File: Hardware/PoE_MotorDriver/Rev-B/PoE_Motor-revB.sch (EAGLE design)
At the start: 87 parts, among them IC2 ATMEGA32U4-MU, J6 10103594-0001LF, SW1 SPST_TACT-KMR2, T1 DMG3415U, U2 SPX3819-3.3, U3 LMV358IDGKR, U4 W5500, U8 DRV8871, U9 DRV8871, X2 J1011FHANRUN, X3 DCMOTOR, X4 DCMOTOR, Y4 8MHz

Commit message: HEEP-614 finished rev b motor driver
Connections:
- removed net 10: J4.1, U8.IN1
- removed net 5: J2.1, U8.IN2
- removed net 6: J5.1, U9.IN1
- removed net 9: J3.1, U9.IN2
- net EN1: now also D1.A, J2.1, U8.IN2
- net EN2: now also D2.A, J4.1, U8.IN1
- net EN3: now also D3.A, J3.1, U9.IN2
- net EN4: now also D4.A, J5.1, U9.IN1
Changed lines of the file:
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@@
 </segment>
 </net>
-<net name="5" class="0">
+<net name="EN1" class="0">
 <segment>
 <pinref part="U8" gate="G$1" pin="IN2"/>
-<wire x1="375.92" y1="215.9" x2="353.06" y2="215.9" width="0.1524" layer="91"/>
+<wire x1="375.92" y1="215.9" x2="365.76" y2="215.9" width="0.1524" layer="91"/>
 <pinref part="J2" gate="G$1" pin="1"/>
+<label x="360.68" y="215.9" size="1.778" layer="95"/>
+<pinref part="D1" gate="G$1" pin="A"/>
+<wire x1="365.76" y1="215.9" x2="353.06" y2="215.9" width="0.1524" layer="91"/>
+<junction x="365.76" y="215.9"/>
 </segment>
 </net>
-<net name="10" class="0">
+<net name="EN2" class="0">
 <segment>
 <pinref part="U8" gate="G$1" pin="IN1"/>
-<wire x1="375.92" y1="213.36" x2="353.06" y2="213.36" width="0.1524" layer="91"/>
+<wire x1="375.92" y1="213.36" x2="365.76" y2="213.36" width="0.1524" layer="91"/>
 <label x="360.68" y="213.36" size="1.778" layer="95"/>
 <pinref part="J4" gate="G$1" pin="1"/>
+<pinref part="D2" gate="G$1" pin="A"/>
+<wire x1="365.76" y1="213.36" x2="353.06" y2="213.36" width="0.1524" layer="91"/>
+<junction x="365.76" y="213.36"/>
 </segment>
 </net>
-<net name="9" class="0">
+<net name="EN3" class="0">
 <segment>
 <pinref part="U9" gate="G$1" pin="IN2"/>
-<wire x1="373.38" y1="167.64" x2="347.98" y2="167.64" width="0.1524" layer="91"/>
+<wire x1="373.38" y1="167.64" x2="358.14" y2="167.64" width="0.1524" layer="91"/>
 <label x="360.68" y="167.64" size="1.778" layer="95"/>
 <pinref part="J3" gate="G$1" pin="1"/>
+<pinref part="D3" gate="G$1" pin="A"/>
+<wire x1="358.14" y1="167.64" x2="347.98" y2="167.64" width="0.1524" layer="91"/>
+<junction x="358.14" y="167.64"/>
 </segment>
 </net>
-<net name="6" class="0">
+<net name="EN4" class="0">
 <segment>
 <pinref part="U9" gate="G$1" pin="IN1"/>
-<wire x1="373.38" y1="165.1" x2="347.98" y2="165.1" width="0.1524" layer="91"/>
+<wire x1="373.38" y1="165.1" x2="358.14" y2="165.1" width="0.1524" layer="91"/>
 <label x="360.68" y="165.1" size="1.778" layer="95"/>
 <pinref part="J5" gate="G$1" pin="1"/>
+<pinref part="D4" gate="G$1" pin="A"/>
+<wire x1="358.14" y1="165.1" x2="347.98" y2="165.1" width="0.1524" layer="91"/>
+<junction x="358.14" y="165.1"/>
 </segment>
 </net>

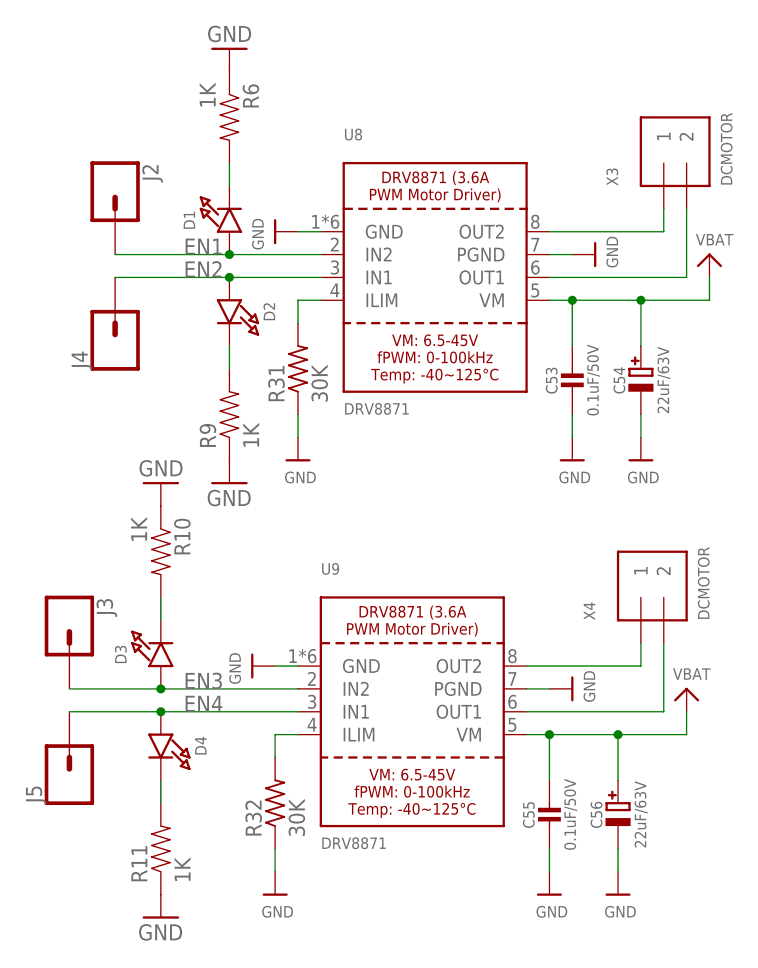
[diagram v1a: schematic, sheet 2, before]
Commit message: HEEP-651 updated capacitor voltage ratings to reflect true minimum requirements
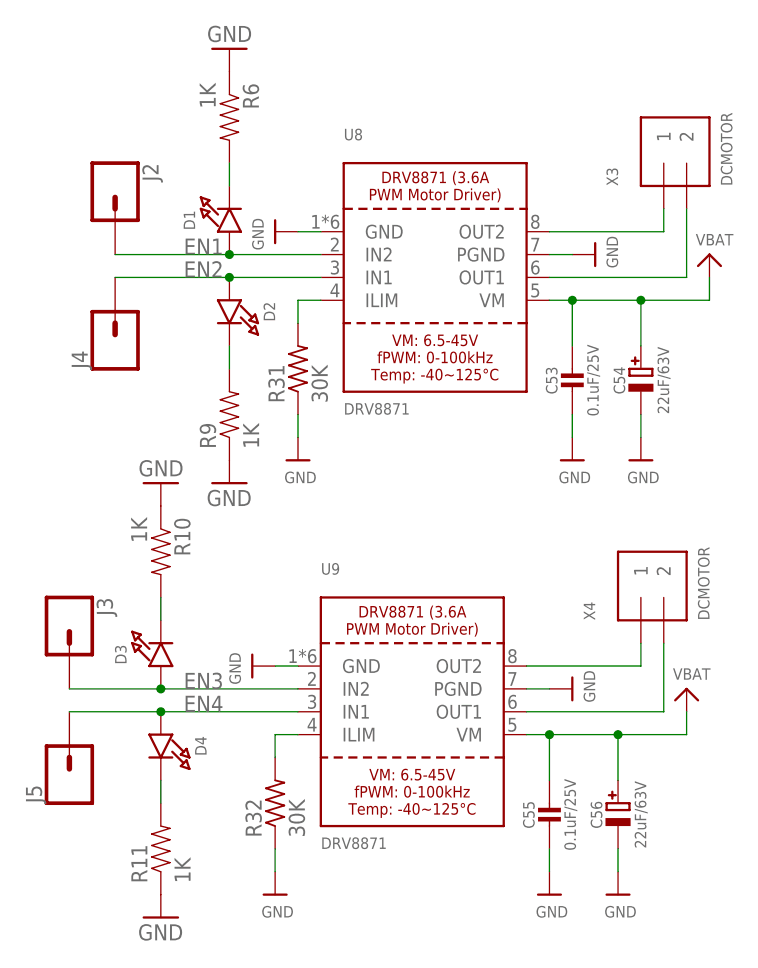
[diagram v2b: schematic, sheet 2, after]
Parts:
- C4: value 10µF 50V -> 10µF 25V
- C53, C55: value 0.1uF/50V -> 0.1uF/25V
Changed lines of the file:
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@@
 <part name="P+2" library="supply1" deviceset="+5V" device=""/>
 <part name="U$19" library="Heep" deviceset="BUCK_CONVERTER" device=""/>
-<part name="C4" library="microbuilder" deviceset="CAP_CERAMIC" device="0603MINI" value="10µF 50V"/>
+<part name="C4" library="microbuilder" deviceset="CAP_CERAMIC" device="0603MINI" value="10µF 25V"/>
 <part name="U$20" library="microbuilder" deviceset="GND" device=""/>
 <part name="U$22" library="microbuilder" deviceset="GND" device=""/>
@@
 <part name="+3V13" library="supply1" deviceset="+3V3" device=""/>
 <part name="U8" library="microbuilder" deviceset="DRV8871" device="" value="DRV8871"/>
-<part name="C53" library="microbuilder" deviceset="CAP_CERAMIC" device="0603_NO" value="0.1uF/50V"/>
+<part name="C53" library="microbuilder" deviceset="CAP_CERAMIC" device="0603_NO" value="0.1uF/25V"/>
 <part name="C54" library="microbuilder" deviceset="CAP_ELECTROLYTIC" device="PANASONIC_D" value="22uF/63V"/>
 <part name="U$50" library="microbuilder" deviceset="GND" device=""/>
@@
 <part name="U$55" library="microbuilder" deviceset="VBAT" device=""/>
 <part name="U9" library="microbuilder" deviceset="DRV8871" device="" value="DRV8871"/>
-<part name="C55" library="microbuilder" deviceset="CAP_CERAMIC" device="0603_NO" value="0.1uF/50V"/>
+<part name="C55" library="microbuilder" deviceset="CAP_CERAMIC" device="0603_NO" value="0.1uF/25V"/>
 <part name="C56" library="microbuilder" deviceset="CAP_ELECTROLYTIC" device="PANASONIC_D" value="22uF/63V"/>
 <part name="U$56" library="microbuilder" deviceset="GND" device=""/>
